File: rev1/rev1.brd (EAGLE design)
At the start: 100 x 80 mm, 38 parts, among them IC1 ATMEGA168-AU, IC2 5v, IC3 74AHC1G04DBV, Q1 MOSFET-NCHANNEL-IRLR3705ZPBF, Q2 MOSFET-PCHANNEL, Q3 MOSFET-NCHANNELBSS138, Y1 16MHz

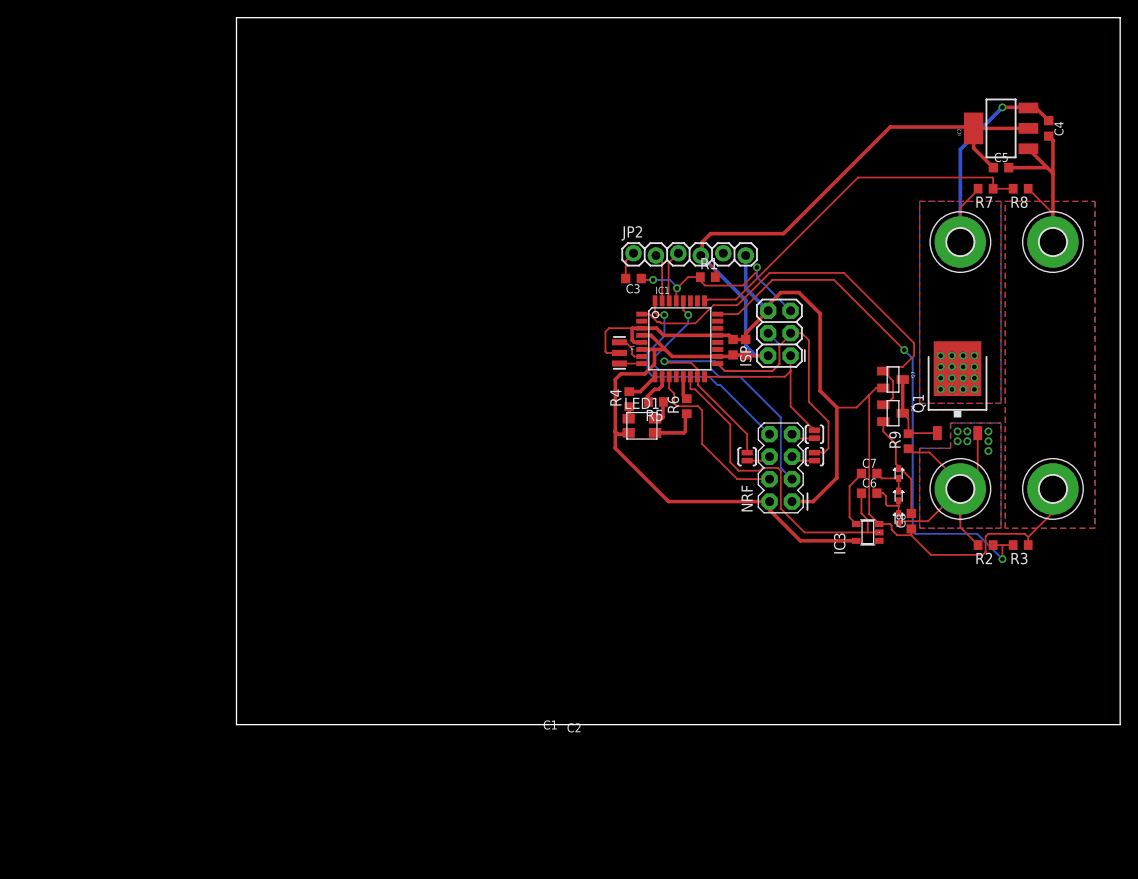
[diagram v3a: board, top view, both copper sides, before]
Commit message: Fixing LDO input pin
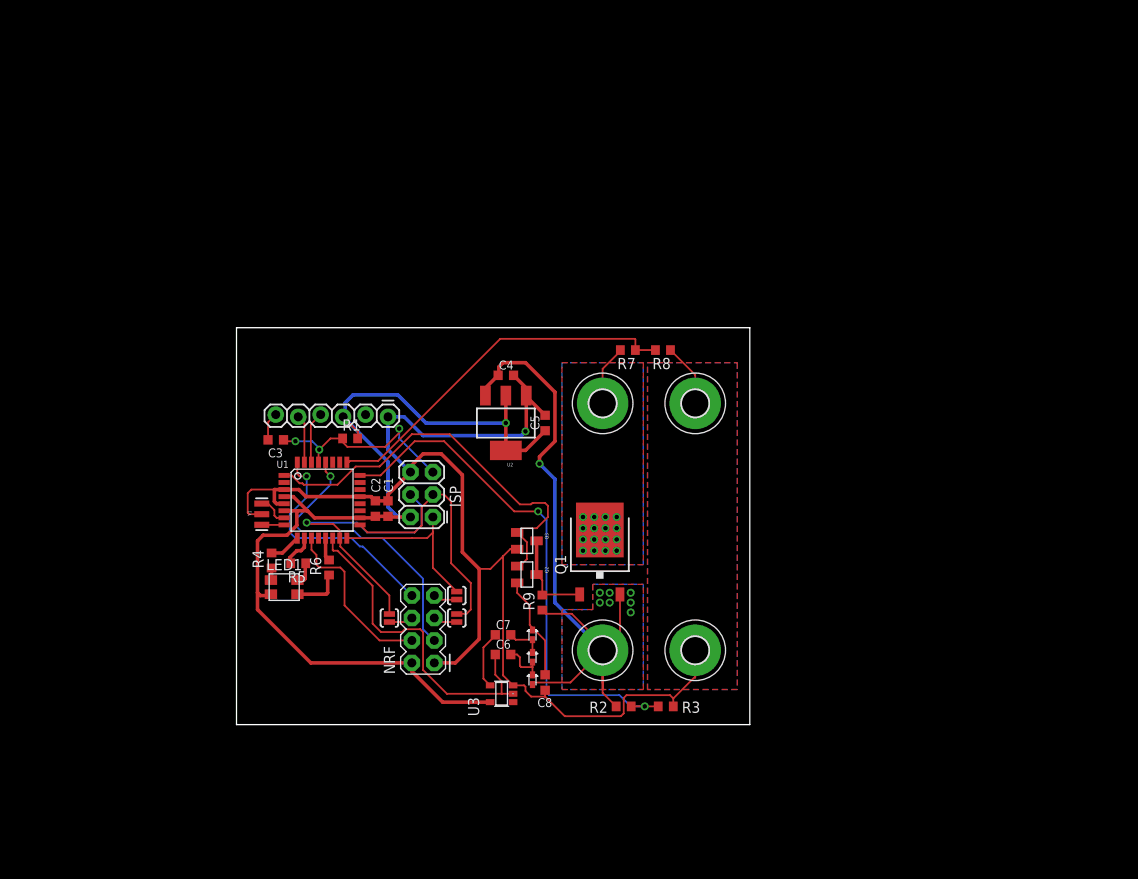
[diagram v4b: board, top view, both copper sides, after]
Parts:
- removed IC1: ATMEGA168-AU, Arduino-AVR:TQFP32-08
- removed IC2: 5v, SparkFun-PowerIC:SOT223
- removed IC3: 74AHC1G04DBV, 74xx-little-de:SOT23-5
- added U1: ATMEGA168-AU, Arduino-AVR:TQFP32-08
- added U2: 5v, SparkFun-PowerIC:SOT223
- added U3: 74AHC1G04DBV, 74xx-little-de:SOT23-5
- moved C4 67.5 mm to (30.5, 39.5), turned to 0 degrees
- moved C5 59.1 mm to (34.9, 34.1), turned to 90 degrees
- moved C8 45.3 mm to (34.9, 4.76)
- moved D1 45.3 mm to (33.5, 7.62)
- moved D2 45.3 mm to (33.5, 10.2)
- moved D3 45.3 mm to (33.5, 5.08)
- moved Q2 45.3 mm to (32.9, 17.0)
- moved Q3 45.3 mm to (32.9, 20.8)
- moved R9 45.3 mm to (34.6, 13.8)
- moved C6 45.3 mm to (30.2, 7.94)
- moved C7 45.3 mm to (30.2, 10.2)
- moved R2 44.8 mm to (43.8, 2.06)
- moved C1 44.4 mm to (17.1, 24.4)
- moved C3 44.4 mm to (4.45, 32.2)
- moved H1 44.4 mm to (41.4, 36.4)
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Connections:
- net +15V: now also C4.1, U2.3
- net +18V: no longer C4.1, IC2.3
- net +5V: now also U1.18, U1.4, U1.6, U2.2, U2.4, U3.5; no longer IC1.18, IC1.4, IC1.6, IC2.2, IC2.4, IC3.5
- net CE: now also U1.28; no longer IC1.28
- net CSN: now also U1.11; no longer IC1.11
- net FET-DRIVE: now also U1.1; no longer IC1.1
- net GND: now also U1.21, U1.3, U1.5, U2.1, U3.3; no longer IC1.21, IC1.3, IC1.5, IC2.1, IC3.3
- net IRQ: now also U1.32; no longer IC1.32
- net MISO: now also U1.16; no longer IC1.16
- net MOSI: now also U1.15; no longer IC1.15
- net MRXSTX: now also U1.31; no longer IC1.31
- net MTXSRX: now also U1.30; no longer IC1.30
- net N$1: now also U1.8; no longer IC1.8
- net N$2: now also U1.7; no longer IC1.7
- net N$3: now also U1.9; no longer IC1.9
- net N$7: now also U1.10; no longer IC1.10
- net N$9: now also U1.13; no longer IC1.13
- net PUMPA: now also U1.14, U3.2; no longer IC1.14, IC3.2
- net PUMPB: now also U3.4; no longer IC3.4
- net RST: now also U1.29; no longer IC1.29
- net SCK: now also U1.17; no longer IC1.17
- net VBAT-READ: now also U1.24; no longer IC1.24
- net VIN-READ: now also U1.25; no longer IC1.25
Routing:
- net +15V: track 34.7 -> 85.5 mm, vias 7 -> 8
- net +18V: track 30.0 -> 6.91 mm, vias 17 -> 16
- net +5V: track 134.3 -> 117.4 mm, vias 0 -> 1
- net GND: track 149.3 -> 161.5 mm, vias 0 -> 1
- net VBAT-READ: track 62.2 -> 60.8 mm
- net FET-PUMP: track 9.71 -> 10.7 mm
- net PUMPA: track 39.5 -> 38.5 mm
- net FET-DRIVE: track 47.4 -> 46.5 mm
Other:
- board size 100 x 80 mm -> 58.1 x 44.9 mm

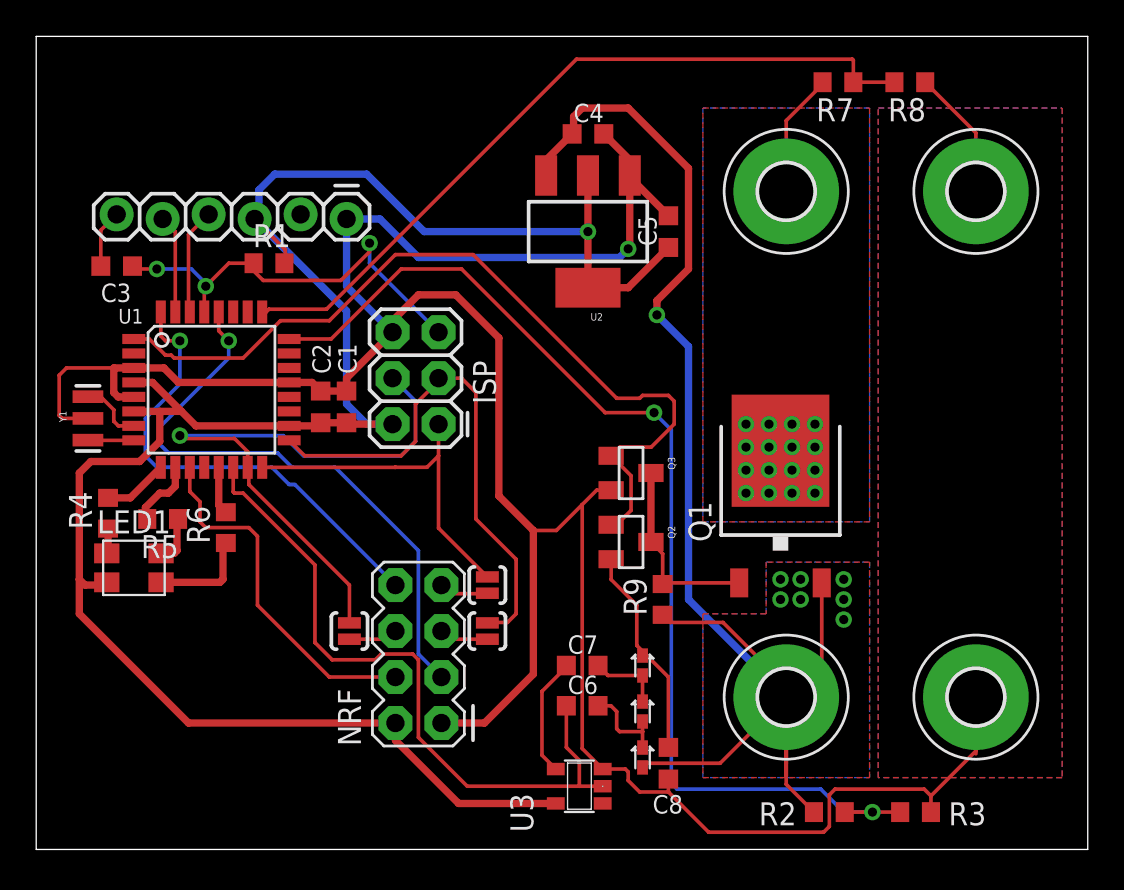
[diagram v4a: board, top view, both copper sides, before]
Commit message: Added copper pour, sorted silk screen
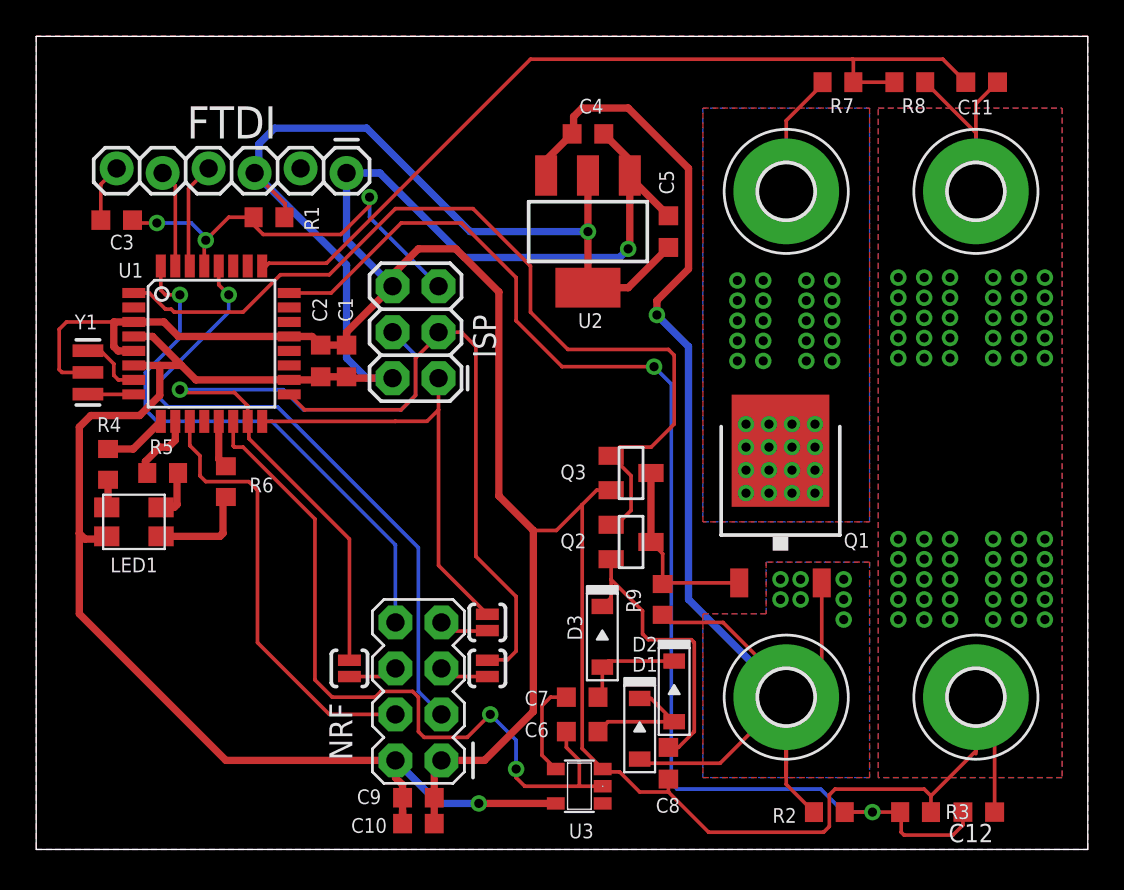
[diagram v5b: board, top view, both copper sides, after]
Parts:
- added C10, C9: 1uF, resistor:C0603K
- added C11, C12: 0.1uF, resistor:C0603K
- D1, D2, D3: value DIODE-SCHOTTKY -> (none); device SparkFun-DiscreteSemi:SOD-523 -> MF_Discrete_Semiconductor:SOD-123
- R2: value 82K -> 82.5K 1%
- R3: value 20K -> 20.1K 1%
- R4, R5: value (none) -> 220R
- R6: value (none) -> 150R
- R7: value (none) -> 82.5K 1%
- R8: value (none) -> 20.1K 1%
- moved D3 7.03 mm to (31.3, 11.7), turned to 270 degrees
- moved R4 2.70 mm to (3.97, 21.3)
- moved U1 2.54 mm to (9.68, 27.9)
- moved LED1 2.54 mm to (5.40, 18.1)
- moved C1 2.54 mm to (17.1, 27.0)
- moved C2 2.54 mm to (15.7, 27.0)
- moved C3 2.54 mm to (4.45, 34.8)
- moved ISP 2.54 mm to (22.2, 26.0)
- moved JP2 2.54 mm to (4.45, 37.6)
- moved R1 2.54 mm to (12.9, 34.9)
- moved R5 2.54 mm to (6.99, 20.8)
- moved R6 2.54 mm to (10.5, 20.3)
- moved Y1 2.54 mm to (2.86, 26.4)
- moved D2 2.26 mm to (35.2, 8.73), turned to 270 degrees
- moved NRF 2.06 mm to (21.1, 8.73)
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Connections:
- net +15V: now also D1.ANODE; no longer D3.A
- net +5V: now also C10.2, C9.2
- net GND: now also C10.1, C11.1, C12.1, C9.1
- net N$10: now also D1.CATHODE, D2.ANODE; no longer D1.A, D3.C
- net N$8: now also D2.CATHODE, D3.ANODE; no longer D1.C, D2.A
- net V+: now also D3.CATHODE; no longer D2.C
- net VBAT-READ: now also C12.2
- net VIN-READ: now also C11.2
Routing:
- net GND: track 161.5 -> 183.8 mm, vias 1 -> 61
- net VBAT-READ: track 60.8 -> 70.2 mm
- net +5V: track 117.4 -> 124.8 mm, vias 1 -> 2
- net VIN-READ: track 42.0 -> 47.7 mm
- net CSN: track 19.8 -> 24.4 mm
- net SCK: track 29.0 -> 33.6 mm
- net MOSI: track 33.7 -> 38.3 mm
- net MISO: track 19.6 -> 24.2 mm
- net IRQ: track 26.4 -> 30.8 mm
- net V+: track 12.0 -> 16.3 mm
- net FET-DRIVE: track 46.5 -> 50.4 mm
- net CE: track 33.3 -> 36.6 mm
- net PUMPA: track 38.5 -> 41.7 mm, vias 0 -> 2
- net N$10: track 5.05 -> 6.87 mm
- net N$8: track 4.13 -> 5.86 mm
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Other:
- board text added: "FTDI"
